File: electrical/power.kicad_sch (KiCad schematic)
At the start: 30 parts

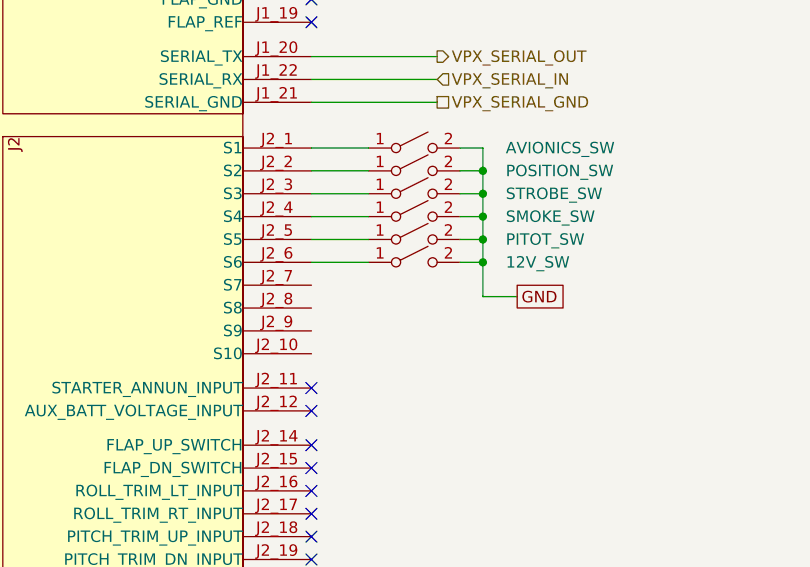
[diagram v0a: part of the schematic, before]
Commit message: Added smoke signal to GEA 24 and moved TOGA to GAD 27
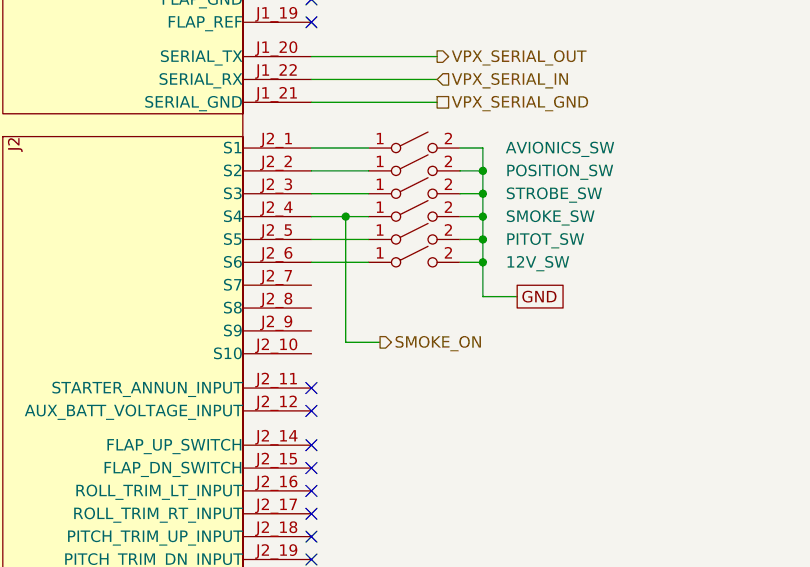
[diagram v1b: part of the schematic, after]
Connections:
- net SMOKE_ON: now reaches SMOKE_SW.1 (A), VPX.J2_4 (S4)
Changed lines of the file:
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@@
   (junction (at 72.39 81.28) (diameter 0) (color 0 0 0 0)
+  )
+  (junction (at 57.15 81.28) (diameter 0) (color 0 0 0 0)
   )
   (junction (at 86.36 200.66) (diameter 0) (color 0 0 0 0)
@@
     (stroke (width 0) (type default))
   )
+  (wire (pts (xy 57.15 81.28) (xy 59.69 81.28))
+    (stroke (width 0) (type default))
+  )
   (wire (pts (xy 78.74 22.86) (xy 78.74 20.32))
     (stroke (width 0) (type default))
@@
     (stroke (width 0) (type default))
   )
+  (wire (pts (xy 57.15 95.25) (xy 57.15 81.28))
+    (stroke (width 0) (type default))
+  )
   (bus (pts (xy 157.48 82.55) (xy 157.48 86.36))
     (stroke (width 0) (type default))
@@
     (stroke (width 0) (type default))
   )
+  (wire (pts (xy 60.96 95.25) (xy 57.15 95.25))
+    (stroke (width 0) (type default))
+  )
   (wire (pts (xy 156.21 58.42) (xy 160.02 58.42))
     (stroke (width 0) (type default))
@@
     (stroke (width 0) (type default))
   )
-  (wire (pts (xy 53.34 81.28) (xy 59.69 81.28))
+  (wire (pts (xy 53.34 81.28) (xy 57.15 81.28))
     (stroke (width 0) (type default))
   )
@@
     (effects (font (size 1.27 1.27)) (justify left))
   )
+  (hierarchical_label "SMOKE_ON" (shape output) (at 60.96 95.25 0) (fields_autoplaced)
+    (effects (font (size 1.27 1.27)) (justify left))
+  )

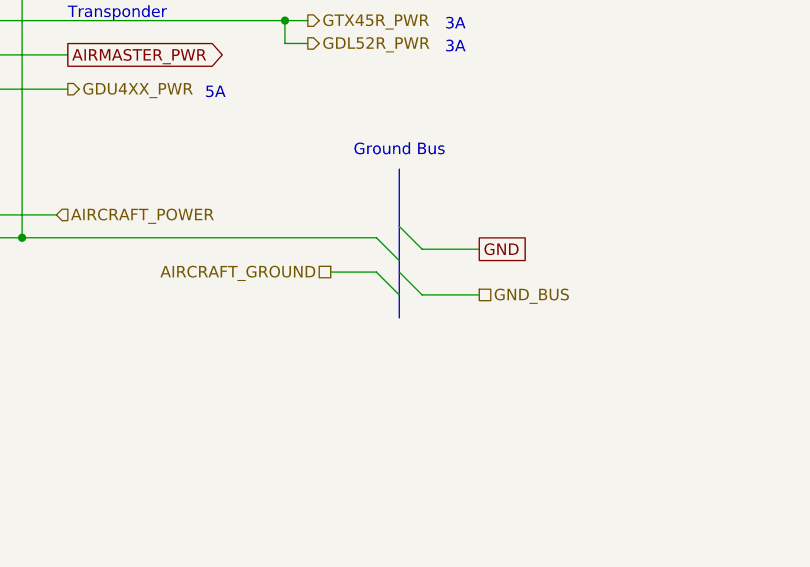
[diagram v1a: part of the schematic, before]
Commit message: Changed grounds and canbuses to be in/out when applicable.
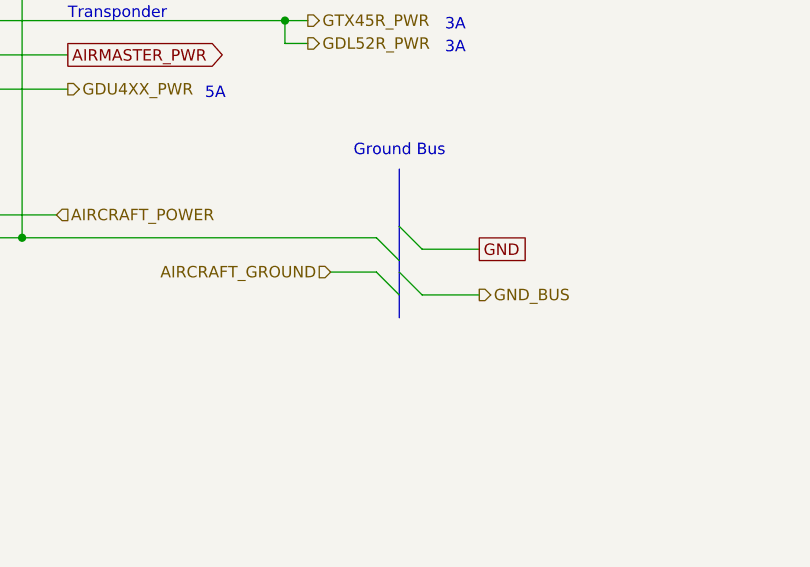
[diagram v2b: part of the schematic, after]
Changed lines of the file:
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@@
     (effects (font (size 1.27 1.27)) (justify left))
   )
-  (hierarchical_label "GND_BUS" (shape passive) (at 107.95 231.14 0) (fields_autoplaced)
+  (hierarchical_label "GND_BUS" (shape output) (at 107.95 231.14 0) (fields_autoplaced)
     (effects (font (size 1.27 1.27)) (justify left))
   )
@@
     (effects (font (size 1.27 1.27)) (justify left))
   )
-  (hierarchical_label "AIRCRAFT_GROUND" (shape passive) (at 91.44 228.6 180) (fields_autoplaced)
+  (hierarchical_label "AIRCRAFT_GROUND" (shape input) (at 91.44 228.6 180) (fields_autoplaced)
     (effects (font (size 1.27 1.27)) (justify right))
   )

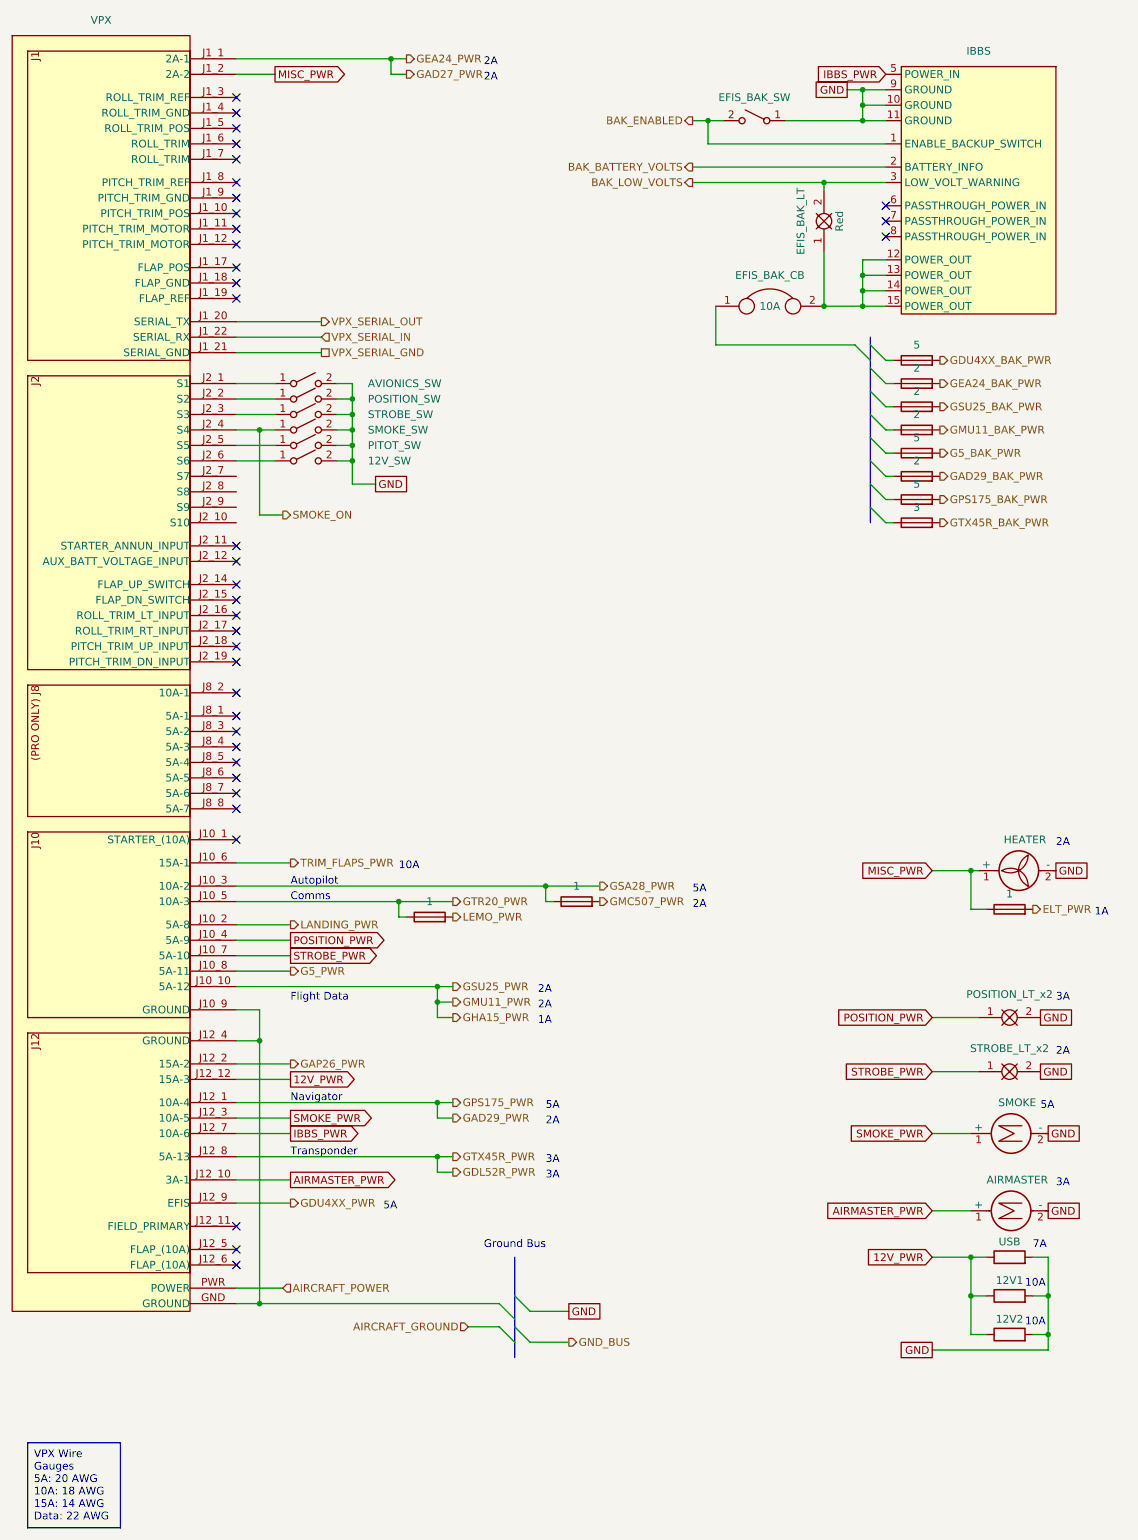
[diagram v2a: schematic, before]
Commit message: Removed GAD 27 and just use VP-X. Not worth it for lights control and better wig-wag. VP-X is good enough and frees up breakers.
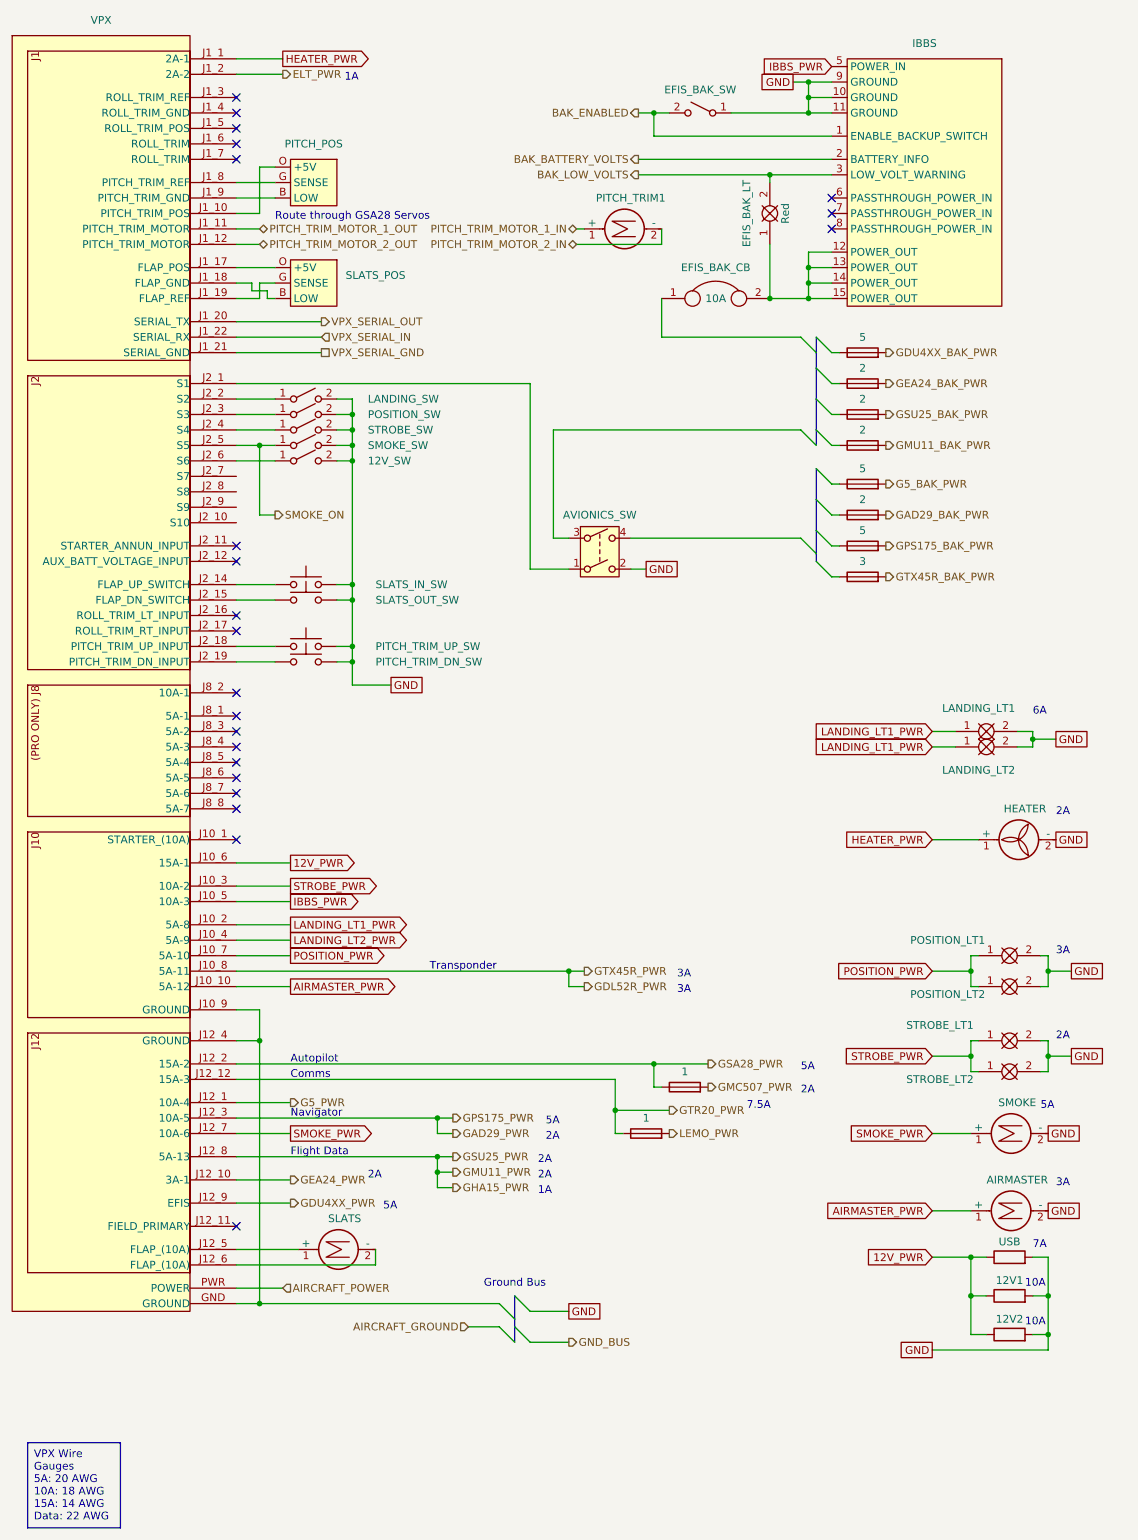
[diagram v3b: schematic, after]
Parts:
- removed AVIONICS_SW: ~, symbol Switch:SW_SPST
- removed ELT_FS: 1, symbol Device:Fuse
- added AVIONICS_SW: SW_DPST, symbol Switch:SW_DPST
- added LANDING_LT1, LANDING_LT2: ~, symbol flyerx:Bulb
- added PITCH_POS, SLATS_POS: ~, symbol flyerx:Ray_Allen_POS-12
- added PITCH_TRIM1, SLATS: Motor_DC, symbol Motor:Motor_DC
- added PITCH_TRIM_DN_SW, PITCH_TRIM_UP_SW, SLATS_IN_SW, SLATS_OUT_SW: SW_Push, symbol Switch:SW_Push
- added POSITION_LT2, STROBE_LT2: Clear, symbol FlyerX:Bulb
- renumbered POSITION_SW to LANDING_SW, POSITION_LT_x2 to POSITION_LT1, STROBE_SW to POSITION_SW, PITOT_SW to SMOKE_SW, STROBE_LT_x2 to STROBE_LT1, SMOKE_SW to STROBE_SW
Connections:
- net GAP26_PWR is gone; now on net GSA28_PWR: VPX.J12_2 (15A-2)
- net TRIM_FLAPS_PWR is gone; now on net 12V_PWR: VPX.J10_6 (15A-1)
- net 12V_PWR: no longer VPX.J12_12 (15A-3)
- net AIRMASTER_PWR: now also VPX.J10_10 (5A-12); no longer VPX.J12_10 (3A-1)
- net ELT_PWR: now also VPX.J1_2 (2A-2)
- net G5_PWR: now also VPX.J12_1 (10A-4); no longer VPX.J10_8 (5A-11)
- net GAD29_PWR: now also VPX.J12_3 (10A-5); no longer VPX.J12_1 (10A-4)
- net GDL52R_PWR: now also VPX.J10_8 (5A-11); no longer VPX.J12_8 (5A-13)
- net GHA15_PWR: now also VPX.J12_8 (5A-13); no longer VPX.J10_10 (5A-12)
- net GND: now also AVIONICS_SW.2, LANDING_LT1.2, LANDING_LT2.2, PITCH_TRIM_DN_SW.2, PITCH_TRIM_UP_SW.2, POSITION_LT2.2, SLATS_IN_SW.2, SLATS_OUT_SW.2, STROBE_LT2.2
- net GSA28_PWR: no longer VPX.J10_3 (10A-2)
- net GTR20_PWR: now also VPX.J12_12 (15A-3); no longer VPX.J10_5 (10A-3)
- net IBBS_PWR: now also VPX.J10_5 (10A-3); no longer VPX.J12_7 (10A-6)
- net POSITION_PWR: now also VPX.J10_7 (5A-10), POSITION_LT2.1; no longer VPX.J10_4 (5A-9)
- net SMOKE_ON: now also SMOKE_SW.1 (A), VPX.J2_5 (S5); no longer STROBE_SW.1 (A), VPX.J2_4 (S4)
- net SMOKE_PWR: now also VPX.J12_7 (10A-6); no longer VPX.J12_3 (10A-5)
- net STROBE_PWR: now also VPX.J10_3 (10A-2), STROBE_LT2.1; no longer VPX.J10_7 (5A-10)
- net at VPX.J2_1 (S1): now also AVIONICS_SW.1
- net at VPX.J12_5 (FLAP_(10A)): now also SLATS.1 (+)
- net at VPX.J12_6 (FLAP_(10A)): now also SLATS.2 (-)
- net at VPX.J1_10 (PITCH_TRIM_POS): now also PITCH_POS.O (+5V)
- net PITCH_TRIM_MOTOR_1_OUT: now reaches VPX.J1_11 (PITCH_TRIM_MOTOR)
- net PITCH_TRIM_MOTOR_2_OUT: now reaches VPX.J1_12 (PITCH_TRIM_MOTOR)
- net at VPX.J1_17 (FLAP_POS): now also SLATS_POS.O (+5V)
- net at VPX.J1_18 (FLAP_GND): now also SLATS_POS.B (LOW)
- net at VPX.J1_19 (FLAP_REF): now also SLATS_POS.G (SENSE)
- net at VPX.J1_8 (PITCH_TRIM_REF): now also PITCH_POS.G (SENSE)
- net at VPX.J1_9 (PITCH_TRIM_GND): now also PITCH_POS.B (LOW)
- net at VPX.J2_14 (FLAP_UP_SWITCH): now also SLATS_IN_SW.1
- net at VPX.J2_15 (FLAP_DN_SWITCH): now also SLATS_OUT_SW.1
- net at VPX.J2_18 (PITCH_TRIM_UP_INPUT): now also PITCH_TRIM_UP_SW.1
- net at VPX.J2_19 (PITCH_TRIM_DN_INPUT): now also PITCH_TRIM_DN_SW.1
- net GAD27_PWR renamed HEATER_PWR
- net HEATER_PWR: now also HEATER.1 (+)
- net LANDING_PWR renamed LANDING_LT1_PWR
- net LANDING_LT1_PWR: now also LANDING_LT1.1, LANDING_LT2.1
- removed net MISC_PWR: HEATER.1 (+), VPX.J1_2 (2A-2)
- new net: STROBE_SW.1 (A), VPX.J2_4 (S4)
- new net GEA24_PWR: VPX.J12_10 (3A-1)
- new net LANDING_LT2_PWR: VPX.J10_4 (5A-9)
- new net PITCH_TRIM_MOTOR_1_IN: PITCH_TRIM1.1 (+)
- new net PITCH_TRIM_MOTOR_2_IN: PITCH_TRIM1.2 (-)
- no-connect marks 36 -> 22
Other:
- note added: "6A"
- note added: "7.5A"
- note added: "Route through GSA28 Servos"
- moved on the sheet: EFIS_BAK_CB, EFIS_BAK_LT, EFIS_BAK_SW, HEATER, IBBS, POSITION_LT1, STROBE_LT1

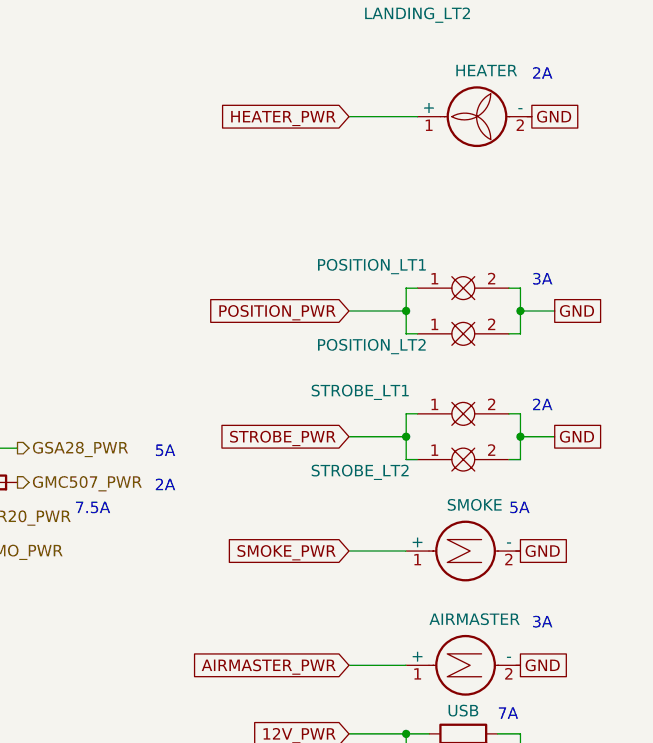
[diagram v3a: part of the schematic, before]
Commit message: Added smoke light.
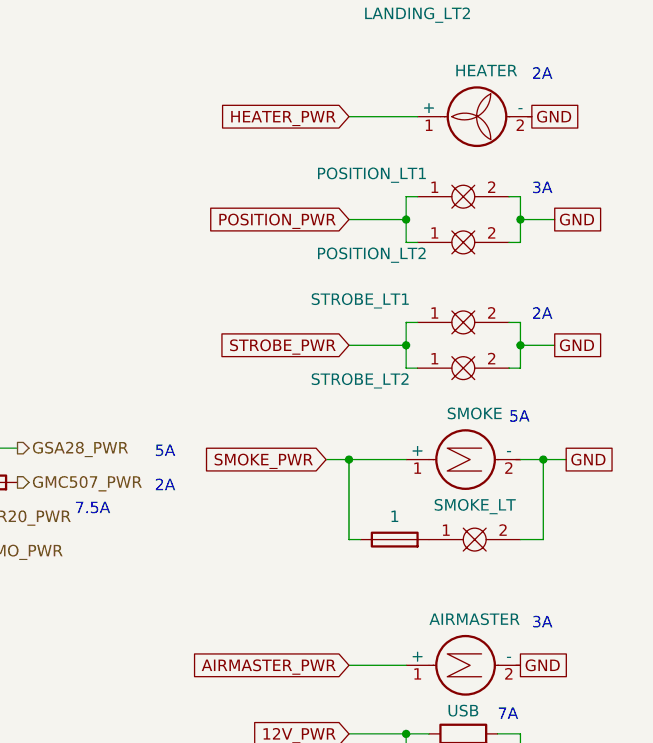
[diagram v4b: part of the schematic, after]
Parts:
- added GMC507_FS1: 1, symbol Device:Fuse
- added SMOKE_LT: ~, symbol flyerx:Bulb
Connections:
- net GND: now also SMOKE_LT.2
- net SMOKE_PWR: now also GMC507_FS1.1
- new net: GMC507_FS1.2, SMOKE_LT.1
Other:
- moved on the sheet: POSITION_LT1, POSITION_LT2, SMOKE, STROBE_LT1, STROBE_LT2

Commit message: Changed smoke power light fuse name
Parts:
- renumbered GMC507_FS1 to SMOKE_LT_FS
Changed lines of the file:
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@@
   (symbol (lib_id "Device:Fuse") (at 172.72 195.58 90) (unit 1)
     (in_bom yes) (on_board yes) (dnp no)
-    (property "Reference" "GMC507_FS1" (at 172.72 191.77 90)
+    (property "Reference" "SMOKE_LT_FS" (at 172.72 191.77 90)
       (effects (font (size 1.27 1.27)) hide)
     )
@@
       (project "electrical"
         (path "/e8ec215a-dbe2-4eba-a577-e50a0a128049/2852c073-fbc9-4469-a6bf-ba3e911c7f5a"
-          (reference "GMC507_FS1") (unit 1)
+          (reference "SMOKE_LT_FS") (unit 1)
         )
       )
